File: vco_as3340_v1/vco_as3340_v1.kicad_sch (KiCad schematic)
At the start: 25 parts, among them J1 Conn_02x05_Odd_Even, U1 LM7805_TO220, U2 L7905, U3 AS3340

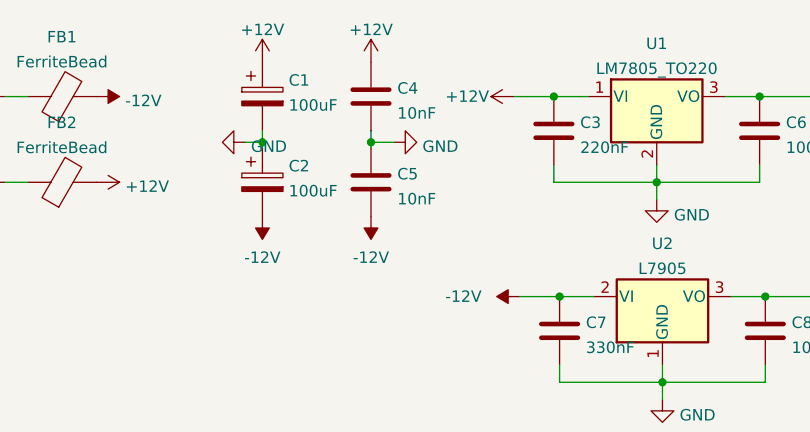
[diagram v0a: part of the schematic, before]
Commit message: Schematic update from breadboarding, start layout
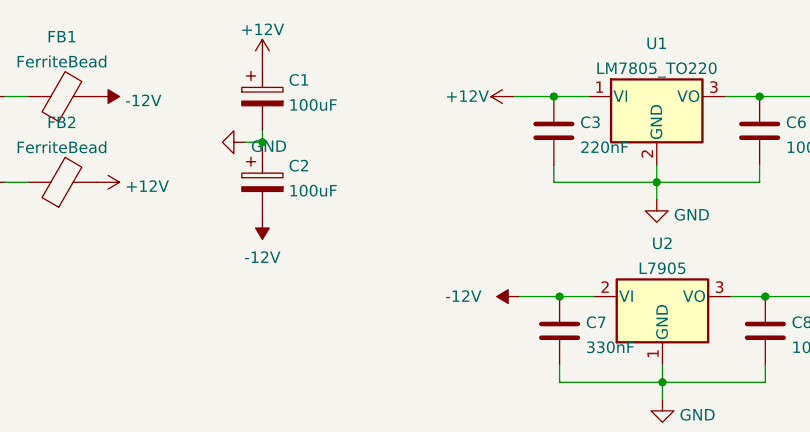
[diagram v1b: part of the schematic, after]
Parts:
- removed C4, C5: 10nF, Capacitor_THT:C_Disc_D6.0mm_W4.4mm_P5.00mm, symbol Device:C
- C10, C3, C6, C7, C8, C9: footprint Capacitor_THT:C_Disc_D6.0mm_W4.4mm_P5.00mm -> Capacitor_SMD:C_1206_3216Metric_Pad1.33x1.80mm_HandSolder
- CF1: footprint Capacitor_THT:C_Disc_D6.0mm_W4.4mm_P5.00mm -> Capacitor_THT:C_Rect_L10.0mm_W2.5mm_P7.50mm_MKS4

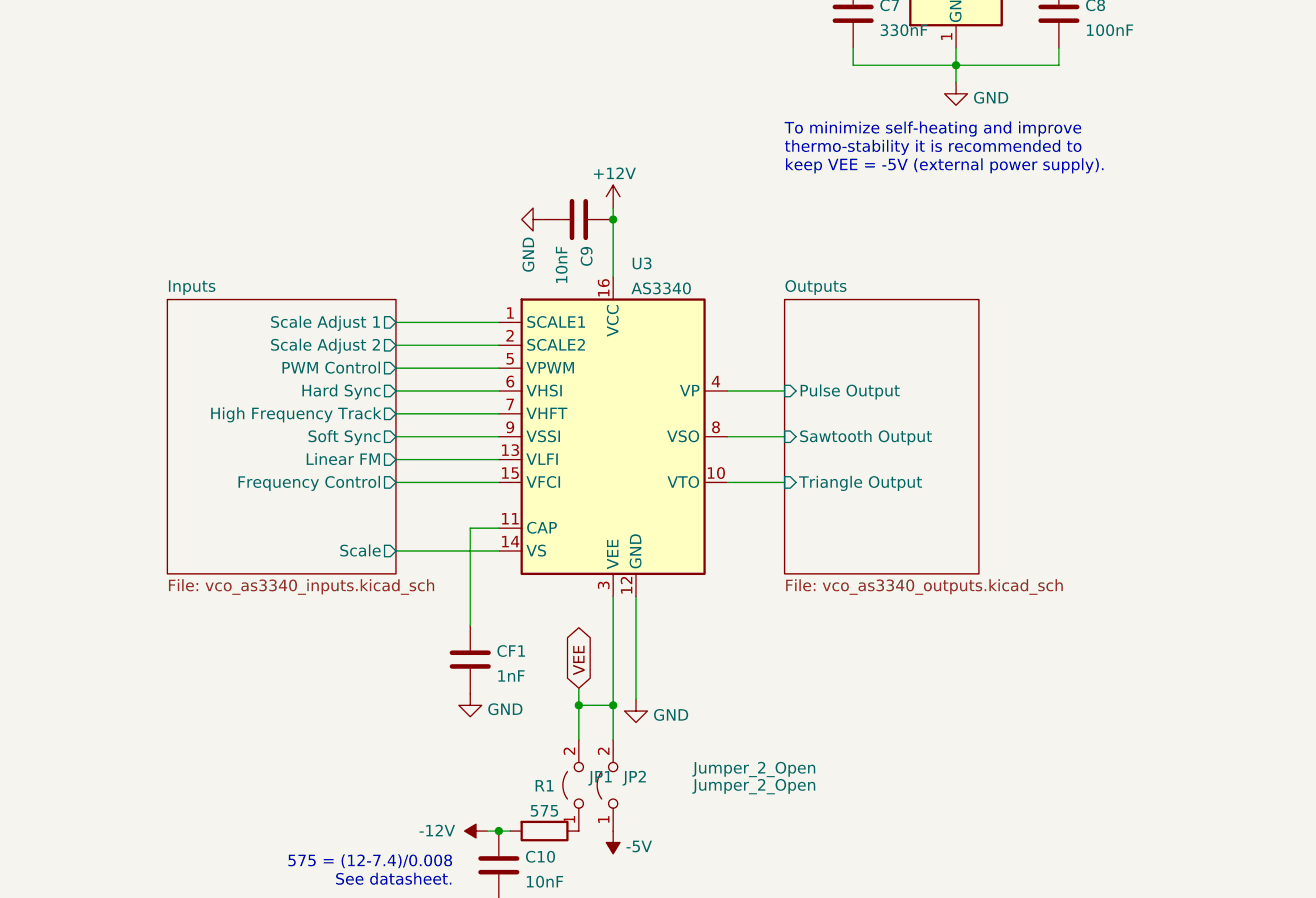
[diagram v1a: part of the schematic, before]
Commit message: Layout and routing done
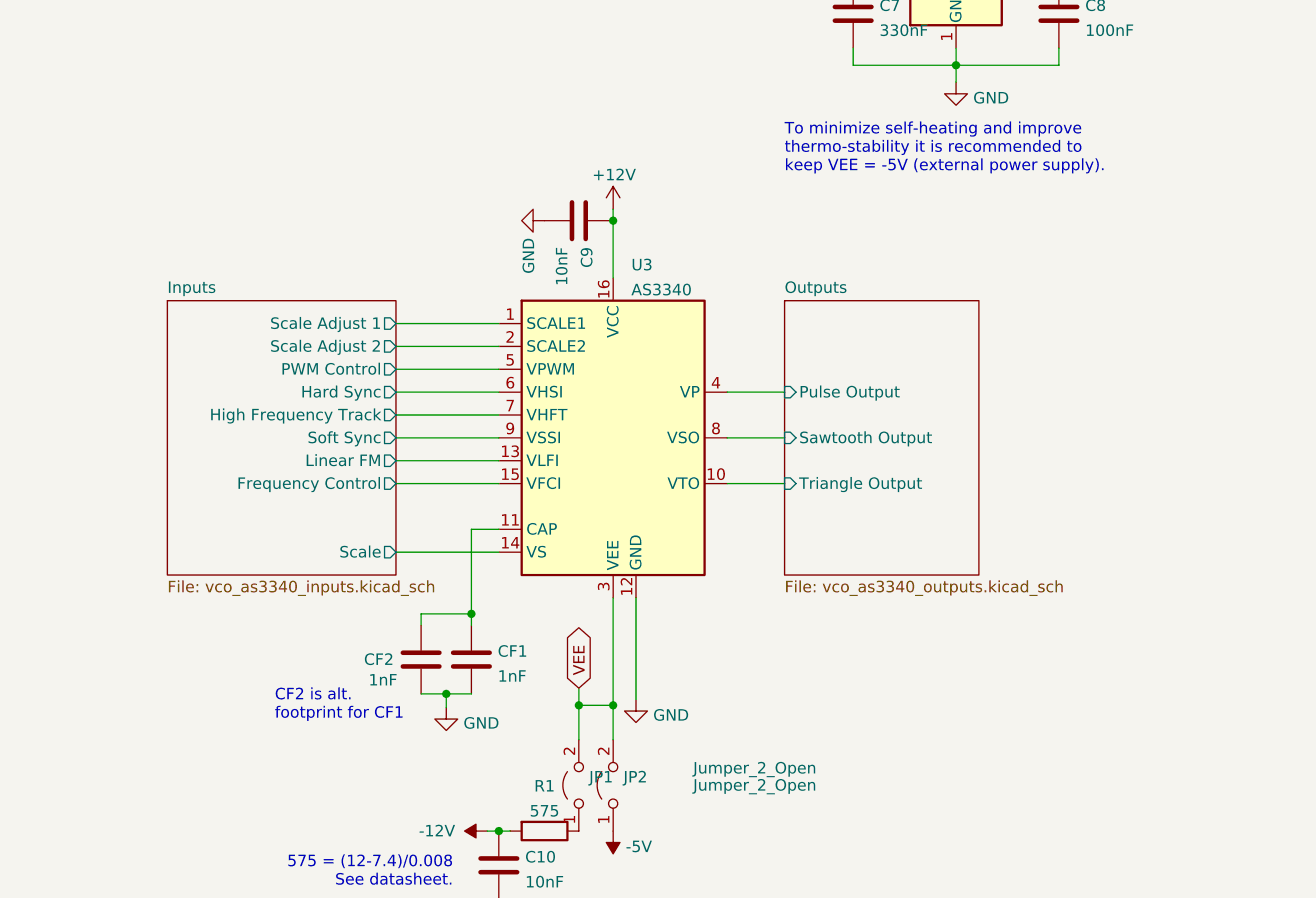
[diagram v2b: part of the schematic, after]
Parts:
- added CF2: 1nF, Capacitor_THT:C_Rect_L7.0mm_W2.5mm_P5.00mm, symbol Device:C
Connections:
- net GND: now also CF2.2
- net at CF1.1, U3.11 (CAP): now also CF2.1
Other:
- note added: "CF2 is alt. footprint for CF1"

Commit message: Geographic re-annotate and cleanup
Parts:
- renumbered C1 to C4, D2 to D1, D3 to D2, J1 to J2, JP1 to JP3, LOGO2 to LOGO101, LOGO3 to LOGO2, R1 to R5

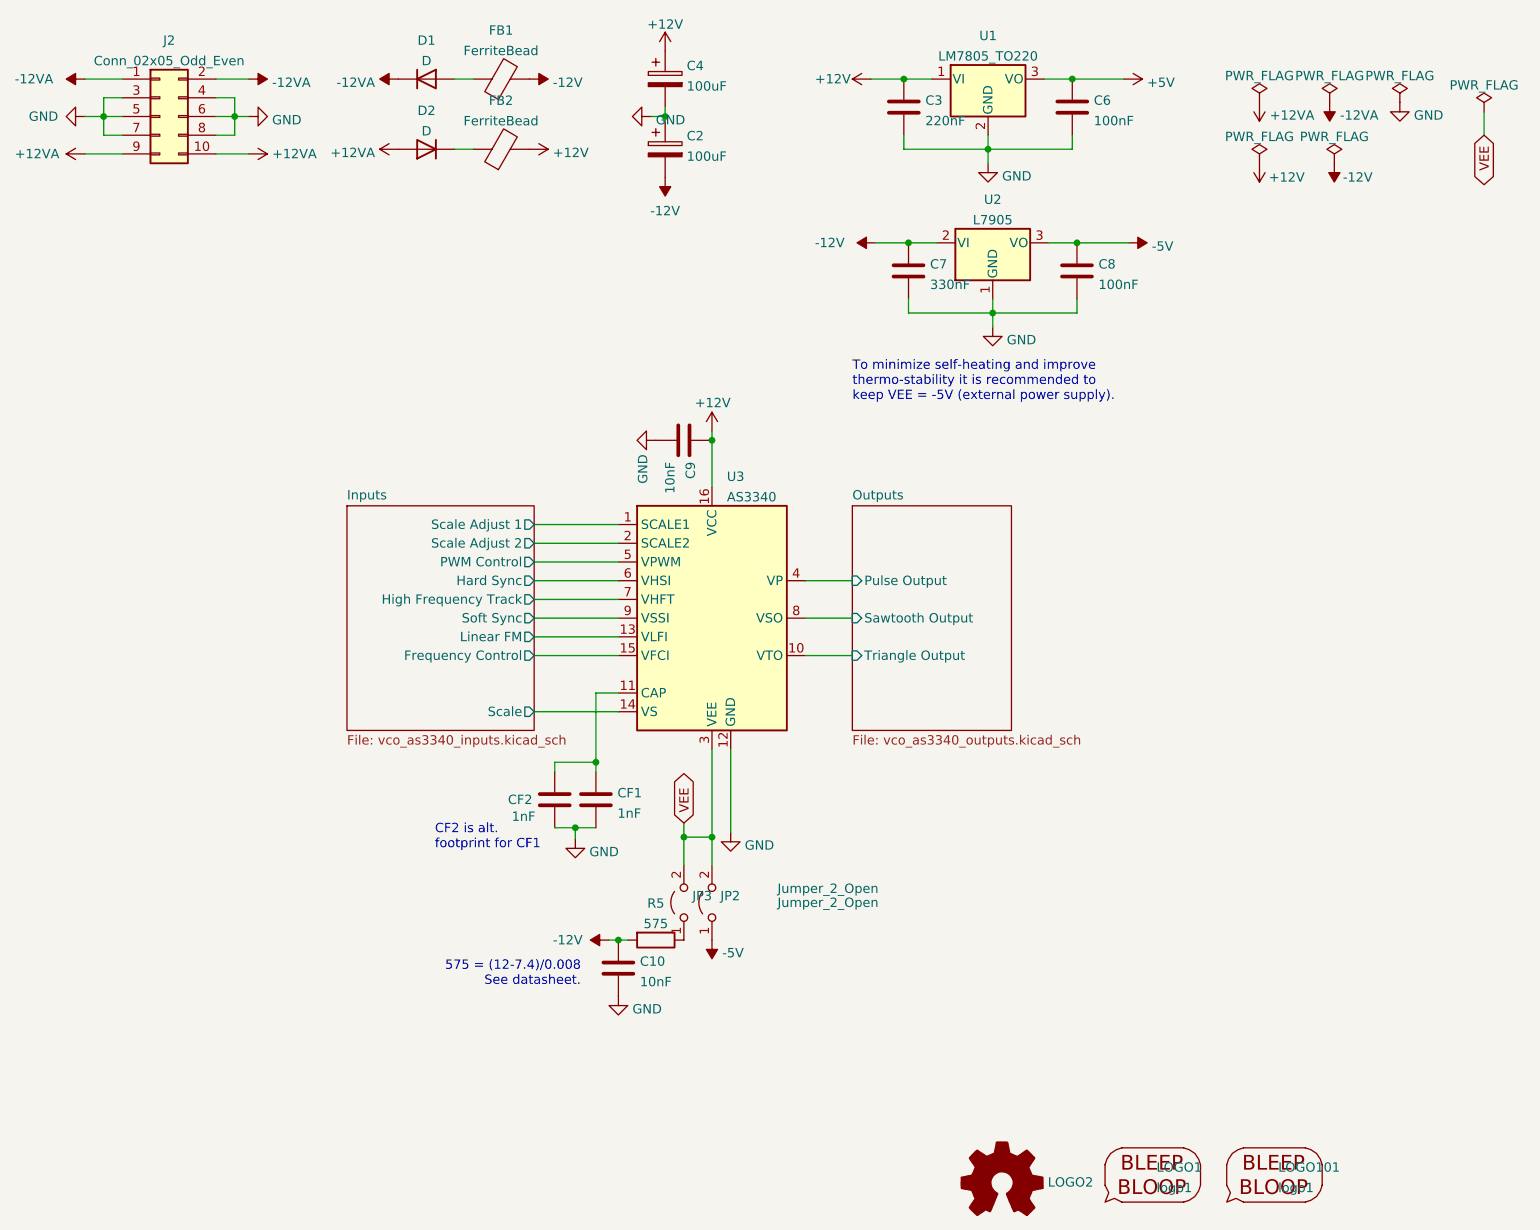
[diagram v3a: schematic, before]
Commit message: Schematic Changes v1 to v2
 - R10 = 47k
 - R9 = 0ohm
 - New C1 100pF across R10 and R9
 - New C15 10uF polarized cap from -5 to GND.
 - R6 DNU
 - R21 & R23 changed to 5.1k
 - RZ1 changed to 18k
 - R26 changed to 100k and new R31 is 100k.
 - New  R32 for 'hysteresis' between PWM and Pulse.
 - Separated grounds on Linear FM and Scale Adj. Circuits for clarity.
 - Added another TL072 (U6) and supporting circuits.
    - This is intended to supply two reference voltages from the 5V
source.
    - The idea is to provide Soft Sync (pin 9) with a stable voltage
of 1/3*Supply, which is something like 11.3/3.
    - The other REF_PITCH2 is for the Linear FM circuit. Some resistors
probably aren't right for this yet, and I think it can completely
replace REF_PITCH pot so I've placed a jumper there to allow either if
it doesn't work out.
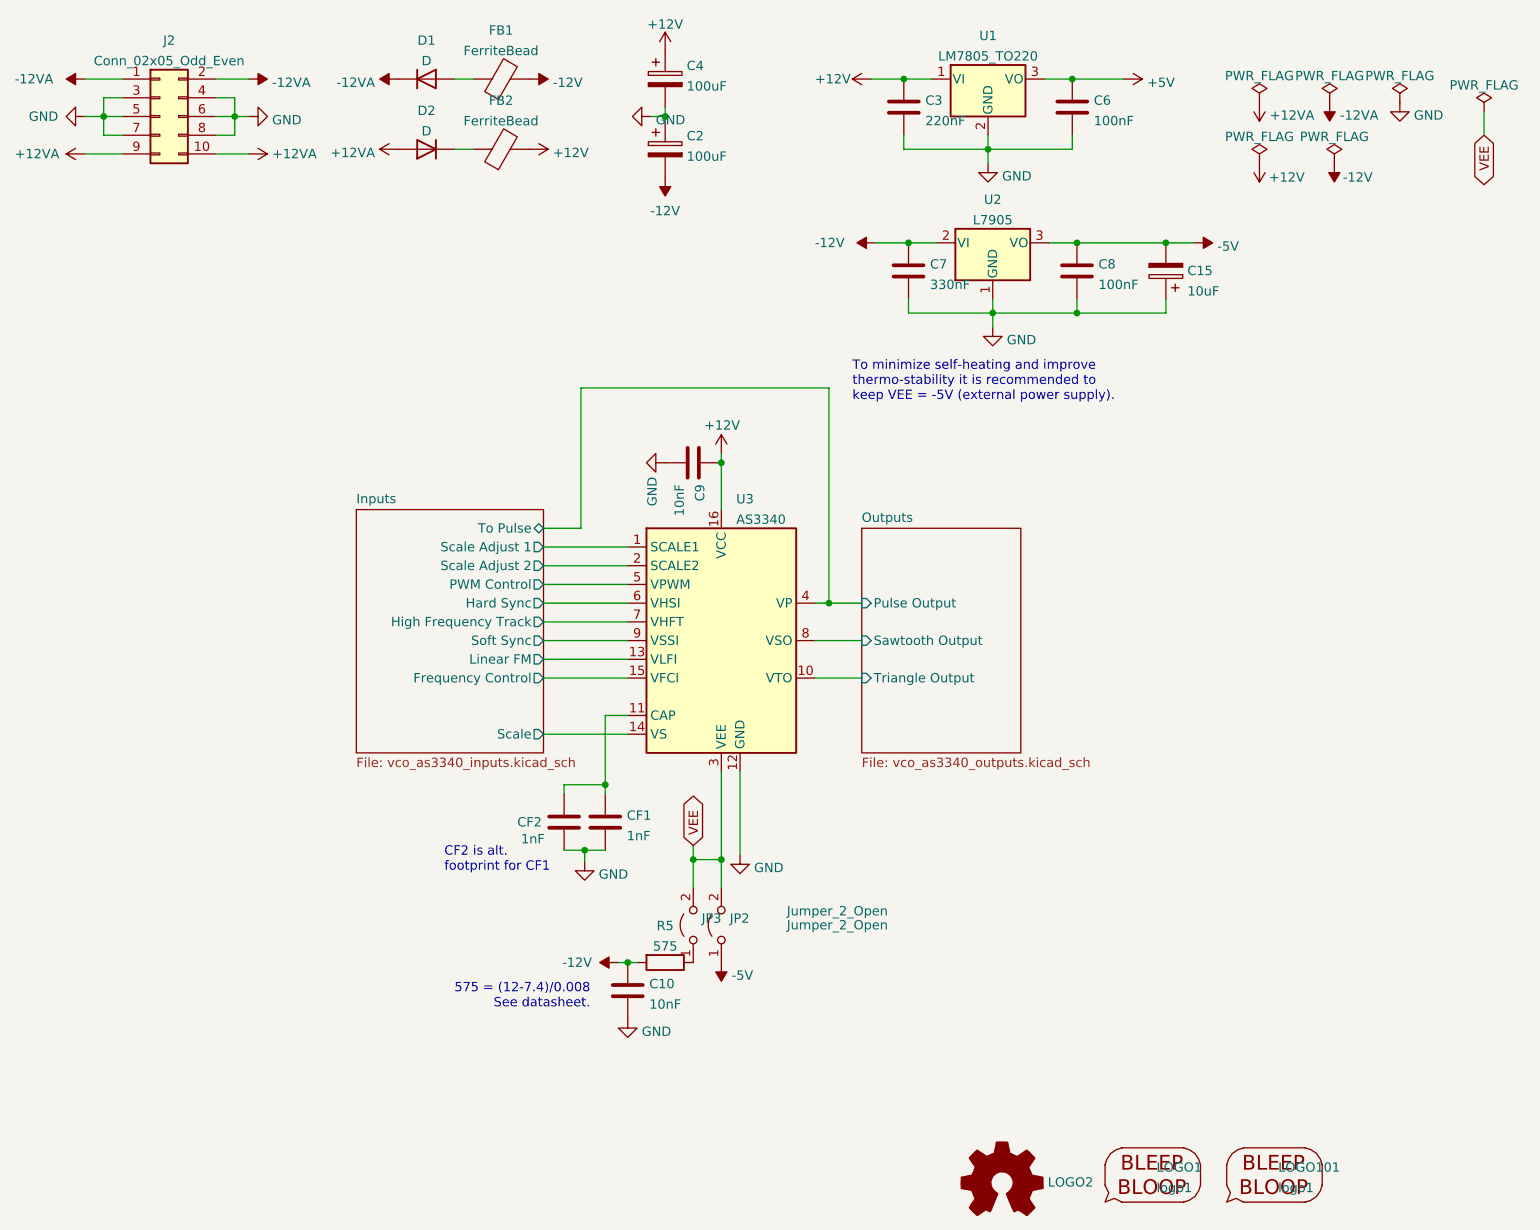
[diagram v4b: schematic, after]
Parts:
- added C15: 10uF, Capacitor_THT:CP_Radial_D5.0mm_P2.50mm, symbol Device:C_Polarized
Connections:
- net -5V: now also C15.2
- net GND: now also C15.1
- net Outputs/Pulse Output renamed Inputs/To Pulse
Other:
- sheet Inputs ports: added To Pulse; removed none
- moved on the sheet: C10, C9, CF1, CF2, JP2, JP3, R5, U3

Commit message: v2 re-layout pcb
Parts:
- removed FB1, FB2: FerriteBead, Inductor_THT:L_Axial_L6.6mm_D2.7mm_P2.54mm_Vertical_Vishay_IM-2, symbol Device:FerriteBead
- removed JP2, JP3: Jumper_2_Open, Connector_PinHeader_2.54mm:PinHeader_1x02_P2.54mm_Vertical, symbol Jumper:Jumper_2_Open
- removed R5: 575, Resistor_SMD:R_1206_3216Metric_Pad1.30x1.75mm_HandSolder, symbol Device:R
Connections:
- net +12V: now also D2.1 (K)
- net -12V: now also D1.2 (A); no longer C10.1
- net -5V: now also C10.1, U3.3 (VEE)
- net VEE: no longer U3.3 (VEE)
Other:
- moved on the sheet: C10
